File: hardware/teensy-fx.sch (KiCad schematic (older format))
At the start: 1 part, among them U1 Teensy4.0

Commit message: initial schematic and parts layout
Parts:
- added H1, H2, H3, H4: MountingHole, MountingHole:MountingHole_3.2mm_M3, symbol Mechanical:MountingHole
- added R3: 100R, Resistor_SMD:R_0805_2012Metric, symbol Device:R
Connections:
- net labels added: +5V, led_clk, led_data, led_latch, led_oe, pot_b0, pot_b1, pot_b2, pot_b3, pot_multiplex, sw_1, sw_2, sw_3, sw_4
- wire segments 1 -> 2
- no-connect marks 0 -> 30
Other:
- note added: "todo\n- battery?"
- moved on the sheet: U1

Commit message: switch to pwm led driver, first pass routing
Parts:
- removed R3: 100R, Resistor_SMD:R_0805_2012Metric, symbol Device:R
- added J3, J4: Conn_01x14, Connector_PinSocket_2.54mm:PinSocket_1x14_P2.54mm_Vertical_SMD_Pin1Left, symbol Connector_Generic:Conn_01x14
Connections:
- wire segments 2 -> 3
- no-connect marks 30 -> 34
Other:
- note added: "audio vol knob"
- note added: "todo\n- try writing code to exercise the chosen peripherals\n"
- note removed: "todo\n- battery?"
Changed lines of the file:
@@
 F1 "SGTL5000.sch" 50
 $EndSheet
-Text GLabel 5100 4700 0    50   Input ~ 0
-SDA
-Text GLabel 5100 4600 0    50   Input ~ 0
-SCL
-Text GLabel 7750 5000 2    50   Input ~ 0
+Text GLabel 7400 5000 2    50   Input ~ 0
 MCLK
-Text GLabel 5100 5100 0    50   Input ~ 0
-BCLK
-Text GLabel 5100 5000 0    50   Input ~ 0
-LRCLK
 Text GLabel 5100 3300 0    50   Input ~ 0
 TX
@@
 EndData
 $EndBitmap
-$Comp
-L Device:R R3
-U 1 1 5E165E4D
-P 7550 5000
-F 0 "R3" V 7343 5000 50  0000 C CNN
-F 1 "100R" V 7434 5000 50  0000 C CNN
-F 2 "Resistor_SMD:R_0805_2012Metric" V 7480 5000 50  0001 C CNN
-F 3 "~" H 7550 5000 50  0001 C CNN
-	1    7550 5000
-	0    1    1    0
-$EndComp
 Wire Wire Line
 	7300 5000 7400 5000
@@
 F1 "pots.sch" 50
 $EndSheet
-Text GLabel 5100 4400 0    50   Input ~ 0
-pot_multiplex
 Text GLabel 5100 2700 0    50   Input ~ 0
 pot_b0
@@
 Text GLabel 5100 3100 0    50   Input ~ 0
 sw_3
-Text GLabel 5100 4300 0    50   Input ~ 0
-sw_4
 Text Notes 8550 1050 0    50   ~ 0
-todo\n- battery?
+todo\n- try writing code to exercise the chosen peripherals\n
 NoConn ~ 7300 4600
 NoConn ~ 7300 5100
@@
 	1    0    0    -1
 $EndComp
+$Comp
+L Connector_Generic:Conn_01x14 J3
+U 1 1 5E1CF1A0
+P 5100 1250
+F 0 "J3" H 5180 1242 50  0000 L CNN
+F 1 "Conn_01x14" H 5180 1151 50  0000 L CNN
+F 2 "Connector_PinSocket_2.54mm:PinSocket_1x14_P2.54mm_Vertical_SMD_Pin1Left" H 5100 1250 50  0001 C CNN
+F 3 "~" H 5100 1250 50  0001 C CNN
+	1    5100 1250
+	1    0    0    -1
+$EndComp
+$Comp
+L Connector_Generic:Conn_01x14 J4
+U 1 1 5E1D05EA
+P 5900 1250
+F 0 "J4" H 5818 2067 50  0000 C CNN
+F 1 "Conn_01x14" H 5818 1976 50  0000 C CNN
+F 2 "Connector_PinSocket_2.54mm:PinSocket_1x14_P2.54mm_Vertical_SMD_Pin1Left" H 5900 1250 50  0001 C CNN
+F 3 "~" H 5900 1250 50  0001 C CNN
+	1    5900 1250
+	-1   0    0    -1
+$EndComp
+Text GLabel 4900 1550 0    50   Input ~ 0
+TX
+Text GLabel 4900 1450 0    50   Input ~ 0
+RX
+$Comp
+L power:GND #PWR0162
+U 1 1 5E1D34FC
+P 4900 650
+AR Path="/5E1D34FC" Ref="#PWR0162"  Part="1"
+AR Path="/5BAC34FB/5E1D34FC" Ref="#PWR?"  Part="1"
+AR Path="/5E0E3867/5E1D34FC" Ref="#PWR?"  Part="1"
+F 0 "#PWR0162" H 4900 400 50  0001 C CNN
+F 1 "GND" V 4905 477 50  0000 C CNN
+F 2 "" H 4900 650 50  0001 C CNN
+F 3 "" H 4900 650 50  0001 C CNN
+	1    4900 650
+	0    1    1    0
+$EndComp
+Text GLabel 4900 950  0    50   Input ~ 0
+pot_b0
+Text GLabel 4900 1050 0    50   Input ~ 0
+pot_b1
+Text GLabel 4900 1150 0    50   Input ~ 0
+pot_b2
+Text GLabel 4900 1250 0    50   Input ~ 0
+pot_b3
+Text GLabel 4900 1950 0    50   Input ~ 0
+led_oe
+Text GLabel 4900 1750 0    50   Input ~ 0
+led_clk
+Text GLabel 4900 1650 0    50   Input ~ 0
+led_data
+Text GLabel 4900 1850 0    50   Input ~ 0
+led_latch
+Text GLabel 4900 750  0    50   Input ~ 0
+sw_1
+Text GLabel 4900 850  0    50   Input ~ 0
+sw_2
+Text GLabel 4900 1350 0    50   Input ~ 0
+sw_3
+Text Notes 4450 4500 0    50   ~ 0
+audio vol knob
+Text GLabel 5100 4300 0    50   Input ~ 0
+sw_4
+Text GLabel 5100 4400 0    50   Input ~ 0
+pot_multiplex
+Text GLabel 5100 5000 0    50   Input ~ 0
+LRCLK
+Text GLabel 5100 5100 0    50   Input ~ 0
+BCLK
+Text GLabel 5100 4600 0    50   Input ~ 0
+SCL
+Text GLabel 5100 4700 0    50   Input ~ 0
+SDA
+Text Notes 6750 1800 2    50   ~ 0
+audio vol knob
+Text GLabel 6100 1950 2    50   Input ~ 0
+sw_4
+Text GLabel 6100 1850 2    50   Input ~ 0
+pot_multiplex
+Text GLabel 6100 1250 2    50   Input ~ 0
+LRCLK
+Text GLabel 6100 1150 2    50   Input ~ 0
+BCLK
+Text GLabel 6100 1650 2    50   Input ~ 0
+SCL
+Text GLabel 6100 1550 2    50   Input ~ 0
+SDA
+Text GLabel 6500 950  2    50   Input ~ 0
+MCLK
+$Comp
+L power:+3V3 #PWR0163
+U 1 1 5E1F128B
+P 6100 850
+AR Path="/5E1F128B" Ref="#PWR0163"  Part="1"
+AR Path="/5BAC34FB/5E1F128B" Ref="#PWR?"  Part="1"
+AR Path="/5E0E3867/5E1F128B" Ref="#PWR?"  Part="1"
+F 0 "#PWR0163" H 6100 700 50  0001 C CNN
+F 1 "+3V3" V 6100 1050 50  0000 C CNN
+F 2 "" H 6100 850 50  0001 C CNN
+F 3 "" H 6100 850 50  0001 C CNN
+	1    6100 850
+	0    1    1    0
+$EndComp
+$Comp
+L power:GND #PWR0164
+U 1 1 5E1F12A1
+P 6100 750
+AR Path="/5E1F12A1" Ref="#PWR0164"  Part="1"
+AR Path="/5BAC34FB/5E1F12A1" Ref="#PWR?"  Part="1"
+AR Path="/5E0E3867/5E1F12A1" Ref="#PWR?"  Part="1"
+F 0 "#PWR0164" H 6100 500 50  0001 C CNN
+F 1 "GND" V 6100 550 50  0000 C CNN
+F 2 "" H 6100 750 50  0001 C CNN
+F 3 "" H 6100 750 50  0001 C CNN
+	1    6100 750
+	0    -1   -1   0
+$EndComp
+$Comp
+L power:+5V #PWR0165
+U 1 1 5E1F12AB
+P 6100 650
+F 0 "#PWR0165" H 6100 500 50  0001 C CNN
+F 1 "+5V" V 6115 778 50  0000 L CNN
+F 2 "" H 6100 650 50  0001 C CNN
+F 3 "" H 6100 650 50  0001 C CNN
+	1    6100 650
+	0    1    1    0
+$EndComp
+Wire Wire Line
+	6100 950  6500 950
+NoConn ~ 6100 1050
+NoConn ~ 6100 1350
+NoConn ~ 6100 1450
+NoConn ~ 6100 1750
 $EndSCHEMATC

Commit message: tidy schematic and finish layout
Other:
- note added: "Teensy 4"
- note added: "todo\n- try writing code to exercise the chosen peripherals\n- check fp of smt headers teensy\n"
- note removed: "todo\n- try writing code to exercise the chosen peripherals\n"
- moved on the sheet: H1, H2, H3, H4, U1

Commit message: made better fp for smt teensy, fixed some wiring errors
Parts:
- removed J3, J4: Conn_01x14, Connector_PinSocket_2.54mm:PinSocket_1x14_P2.54mm_Vertical_SMD_Pin1Left, symbol Connector_Generic:Conn_01x14
- U1: footprint teensy:Teensy40 -> audio-fx:teensy4smt
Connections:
- wire segments 3 -> 2
- no-connect marks 34 -> 30
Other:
- note added: "cs for audio mem"
- moved on the sheet: U1

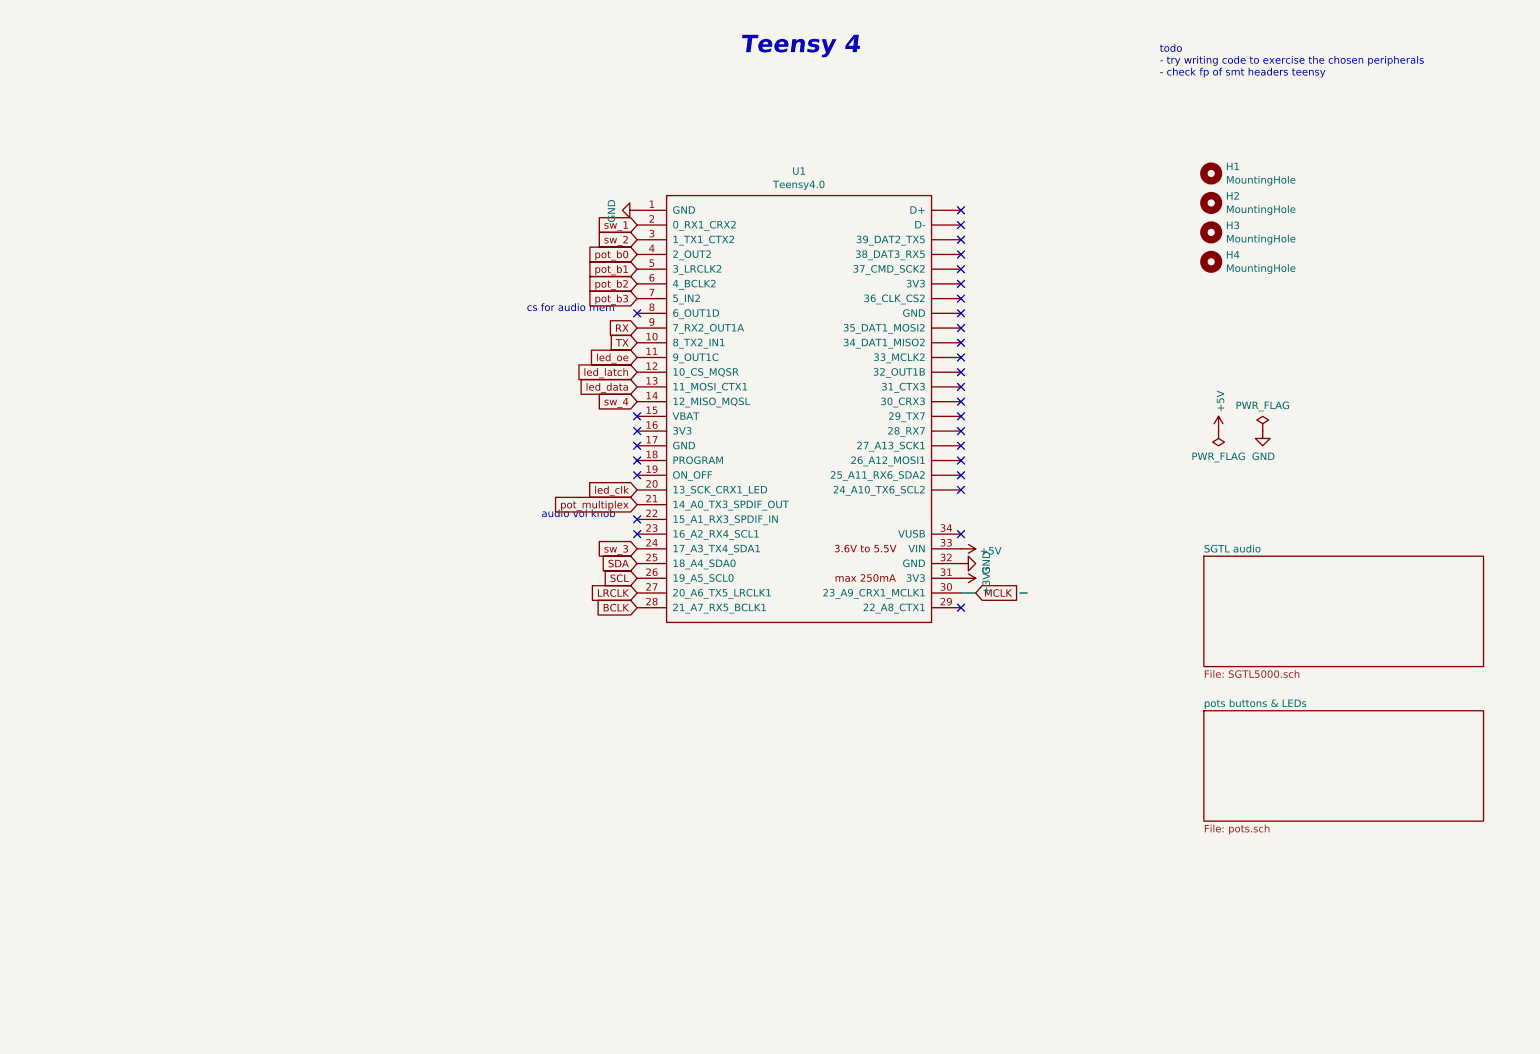
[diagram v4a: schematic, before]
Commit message: move to 4 layer board, change size for cost, add optional flash
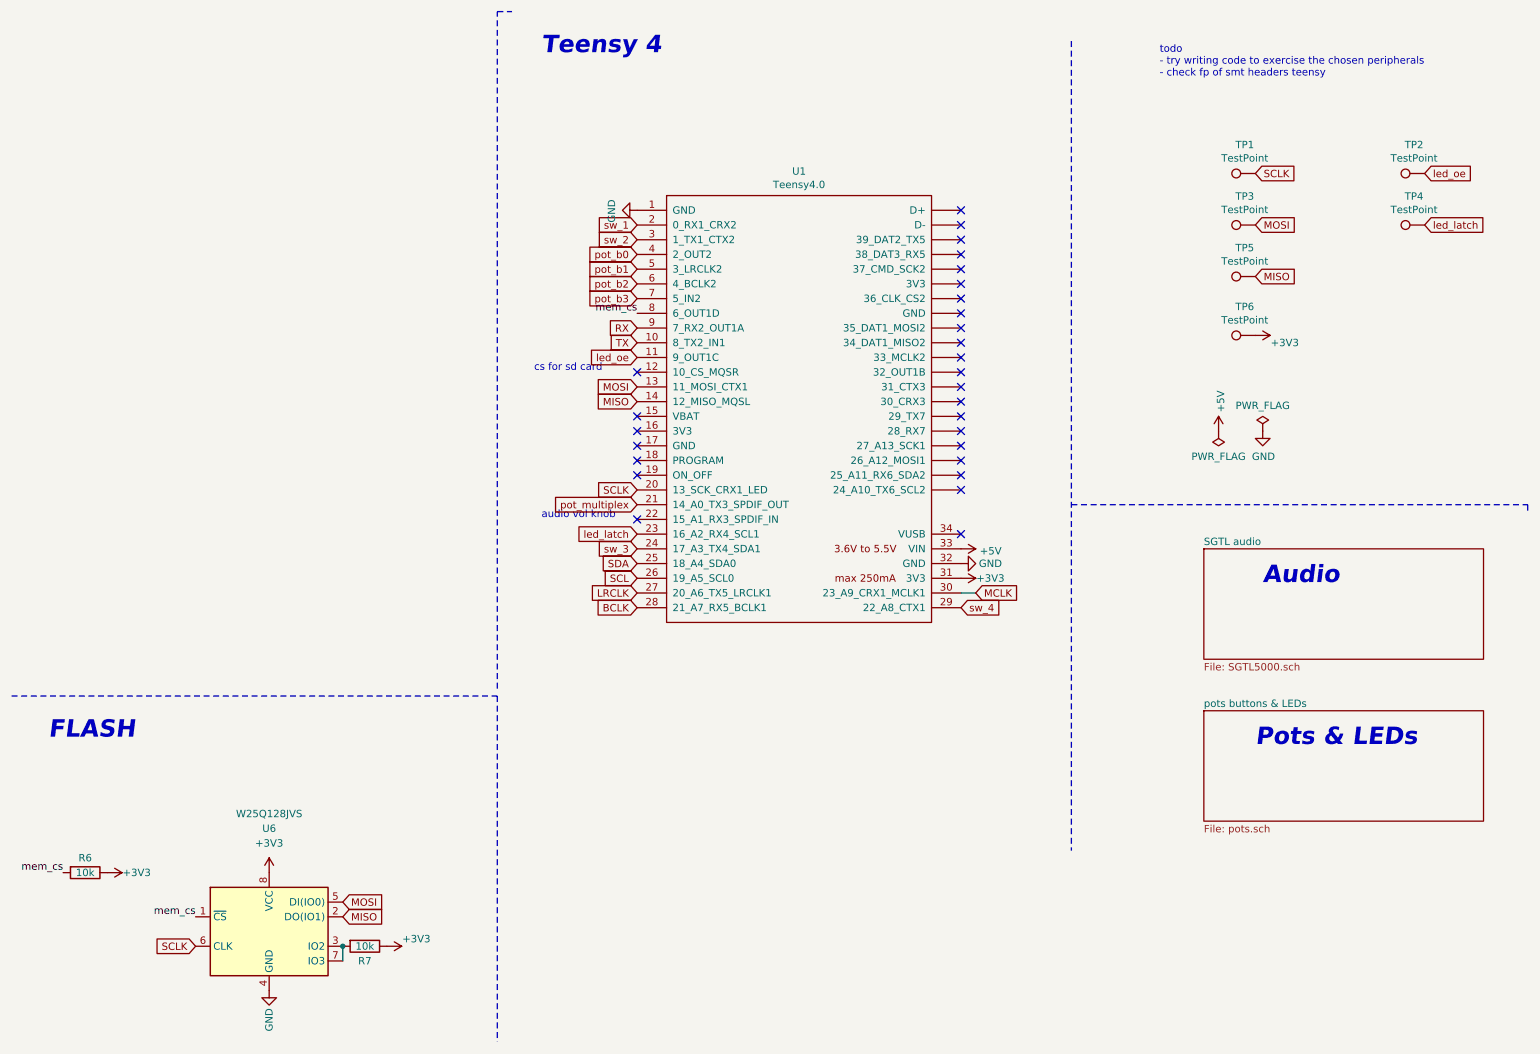
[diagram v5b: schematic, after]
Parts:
- removed H1, H2, H3, H4: MountingHole, MountingHole:MountingHole_3.2mm_M3, symbol Mechanical:MountingHole
- added R6, R7: 10k, Resistor_SMD:R_0805_2012Metric, symbol Device:R
- added TP1, TP2, TP3, TP4, TP5, TP6: TestPoint, TestPoint:TestPoint_Pad_D1.0mm, symbol Connector:TestPoint
- added U6: W25Q128JVS, Package_SO:SOIC-8_5.23x5.23mm_P1.27mm, symbol Memory_Flash:W25Q128JVS
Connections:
- net labels added: MISO, MOSI, SCLK, mem_cs
- net labels removed: led_clk, led_data
- no-connect marks 30 -> 28
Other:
- note added: "Audio"
- note added: "FLASH"
- note added: "Pots & LEDs"
- note added: "cs for sd card"
- note removed: "cs for audio mem"

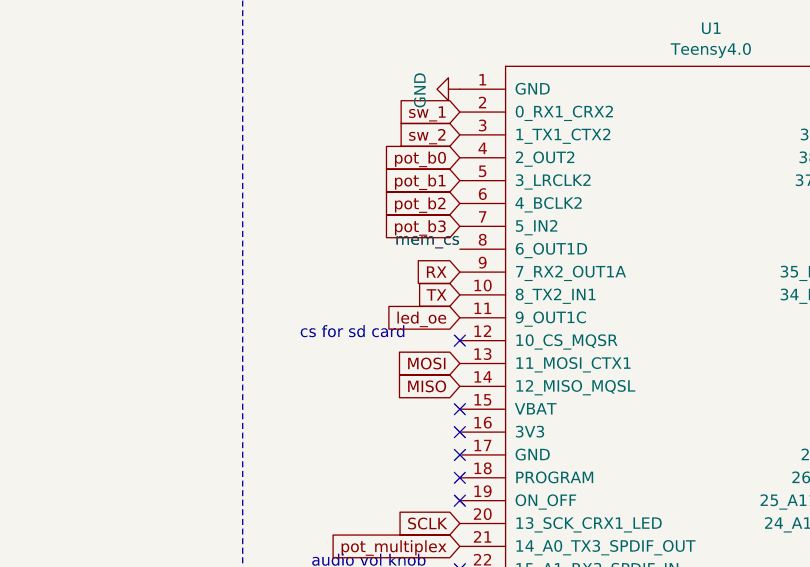
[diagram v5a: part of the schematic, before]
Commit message: fix sgtl5000 symbol error, add filter resistor and cap for unused mic input
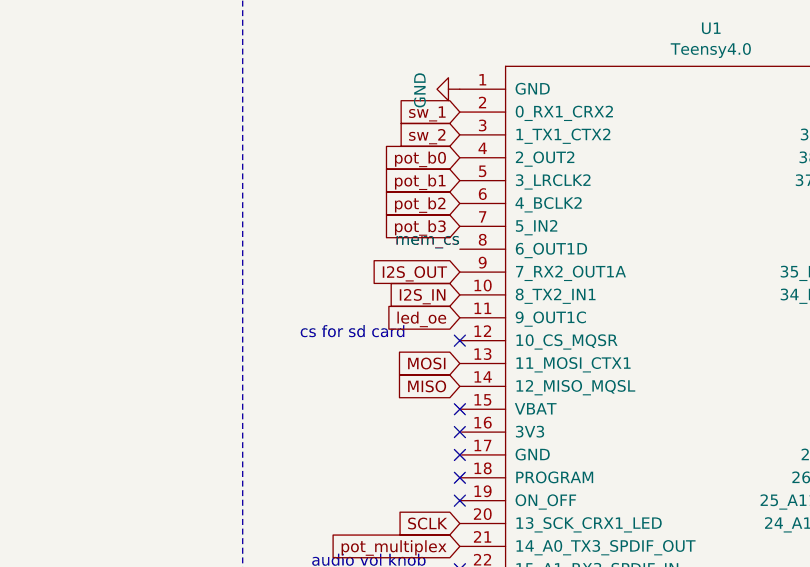
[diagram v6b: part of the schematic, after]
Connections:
- net RX renamed I2S_OUT
- net TX renamed I2S_IN
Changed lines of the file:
@@
 Text GLabel 7300 4550 2    50   Input ~ 0
 MCLK
+Text GLabel 5000 2750 0    50   Input ~ 0
+I2S_OUT
 Text GLabel 5000 2850 0    50   Input ~ 0
-TX
-Text GLabel 5000 2750 0    50   Input ~ 0
-RX
+I2S_IN
 $Comp
 L power:GND #PWR0101

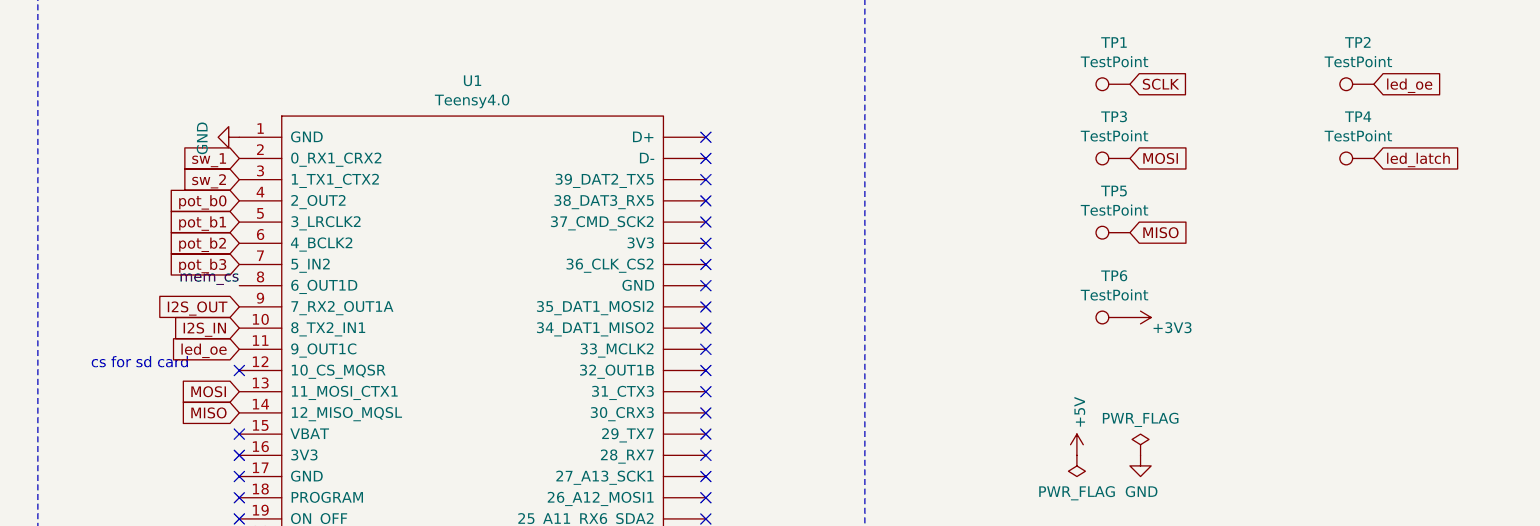
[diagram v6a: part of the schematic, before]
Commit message: new layout following feedback from pjrc forum
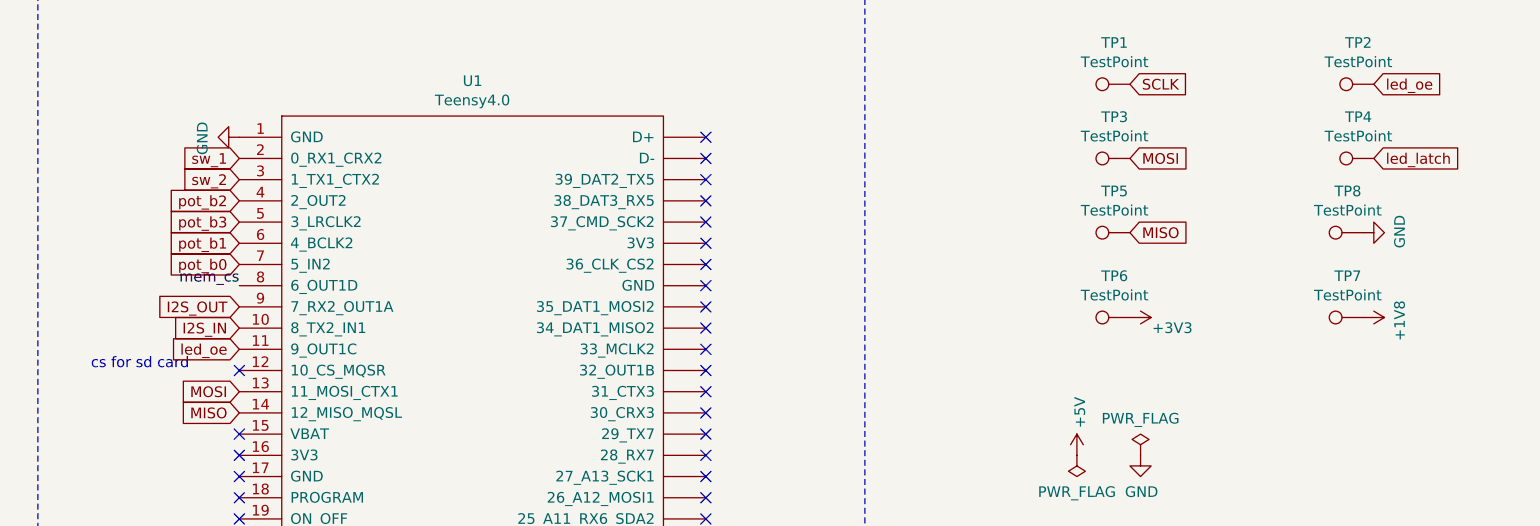
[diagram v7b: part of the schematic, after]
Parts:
- added TP7, TP8: TestPoint, TestPoint:TestPoint_Pad_D1.0mm, symbol Connector:TestPoint
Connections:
- net GND: now also TP8.1
- net pot_b0: now also U1.7 (5_IN2); no longer U1.4 (2_OUT2)
- net pot_b1: now also U1.6 (4_BCLK2); no longer U1.5 (3_LRCLK2)
- net pot_b2: now also U1.4 (2_OUT2); no longer U1.6 (4_BCLK2)
- net pot_b3: now also U1.5 (3_LRCLK2); no longer U1.7 (5_IN2)
- new net +1V8: TP7.1
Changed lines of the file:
@@
 F1 "pots.sch" 50
 $EndSheet
+Text GLabel 5000 2550 0    50   Input ~ 0
+pot_b0
+Text GLabel 5000 2450 0    50   Input ~ 0
+pot_b1
 Text GLabel 5000 2250 0    50   Input ~ 0
-pot_b0
+pot_b2
 Text GLabel 5000 2350 0    50   Input ~ 0
-pot_b1
-Text GLabel 5000 2450 0    50   Input ~ 0
-pot_b2
-Text GLabel 5000 2550 0    50   Input ~ 0
 pot_b3
 Text GLabel 5000 2950 0    50   Input ~ 0
@@
 Text Notes 9200 5600 0    118  Italic 24
 Pots & LEDs
+$Comp
+L Connector:TestPoint TP7
+U 1 1 5E14A287
+P 10300 2800
+F 0 "TP7" V 10495 2872 50  0000 C CNN
+F 1 "TestPoint" V 10404 2872 50  0000 C CNN
+F 2 "TestPoint:TestPoint_Pad_D1.0mm" H 10500 2800 50  0001 C CNN
+F 3 "~" H 10500 2800 50  0001 C CNN
+	1    10300 2800
+	0    -1   -1   0
+$EndComp
+$Comp
+L power:+1V8 #PWR02
+U 1 1 5E14D959
+P 10300 2800
+AR Path="/5E14D959" Ref="#PWR02"  Part="1"
+AR Path="/5BAC34FB/5E14D959" Ref="#PWR?"  Part="1"
+AR Path="/5E0E3867/5E14D959" Ref="#PWR?"  Part="1"
+F 0 "#PWR02" H 10300 2650 50  0001 C CNN
+F 1 "+1V8" H 10315 2973 50  0000 C CNN
+F 2 "" H 10300 2800 50  0001 C CNN
+F 3 "" H 10300 2800 50  0001 C CNN
+	1    10300 2800
+	0    1    1    0
+$EndComp
+$Comp
+L Connector:TestPoint TP8
+U 1 1 5E14E060
+P 10300 2400
+F 0 "TP8" V 10495 2472 50  0000 C CNN
+F 1 "TestPoint" V 10404 2472 50  0000 C CNN
+F 2 "TestPoint:TestPoint_Pad_D1.0mm" H 10500 2400 50  0001 C CNN
+F 3 "~" H 10500 2400 50  0001 C CNN
+	1    10300 2400
+	0    -1   -1   0
+$EndComp
+$Comp
+L power:GND #PWR0167
+U 1 1 5E14E677
+P 10300 2400
+AR Path="/5E14E677" Ref="#PWR0167"  Part="1"
+AR Path="/5BAC34FB/5E14E677" Ref="#PWR?"  Part="1"
+AR Path="/5E0E3867/5E14E677" Ref="#PWR?"  Part="1"
+F 0 "#PWR0167" H 10300 2150 50  0001 C CNN
+F 1 "GND" H 10305 2227 50  0000 C CNN
+F 2 "" H 10300 2400 50  0001 C CNN
+F 3 "" H 10300 2400 50  0001 C CNN
+	1    10300 2400
+	0    -1   -1   0
+$EndComp
 $EndSCHEMATC

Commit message: footprints
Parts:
- U1: farnell (none) -> 2847911
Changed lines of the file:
@@
 F 1 "Teensy4.0" H 6100 4824 50  0000 C CNN
 F 2 "audio-fx:teensy4smt" H 5700 3500 50  0001 C CNN
-F 3 "" H 5700 3500 50  0001 C CNN
+F 3 "https://uk.farnell.com/multicomp/2212sm-14g-75-b1-pcr/connector-rcpt-14pos-1row-2-54mm/dp/2847911" H 5700 3500 50  0001 C CNN
+F 4 "2847911" H 6100 3300 50  0001 C CNN "farnell"
 	1    6100 3300
 	1    0    0    -1
